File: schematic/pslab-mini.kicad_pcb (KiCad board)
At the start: 4 copper layers, 85 x 56 mm, 182 parts, among them J1 USB_C_Receptacle_USB2.0_16P, J2 BAT, J3 Conn_Coaxial, J4 Conn_Coaxial, J5 Conn_02x16_Odd_Even, J6 Conn_01x15_Socket, J7 Conn_02x03_Top_Bottom, Q1 MMBT3904, Q2 MMBT3904, SW1 Reset, SW4 Power, U1 AMS1117-3.3, U10 OPA356AIDBVR, U11 ESP32-C3, U12 W25Q32JV, U2 MT2496, U3 IP5189T, U4 SP0503BAHT, U5 OPA356AIDBVR, U6 OPA356AIDBVR, U7 TLV9001IDCK, U8 STM32H563RIT6, U9 OPA356AIDBVR, X1 32kHz768, Y1 Crystal_25MHz, Y2 40MHz

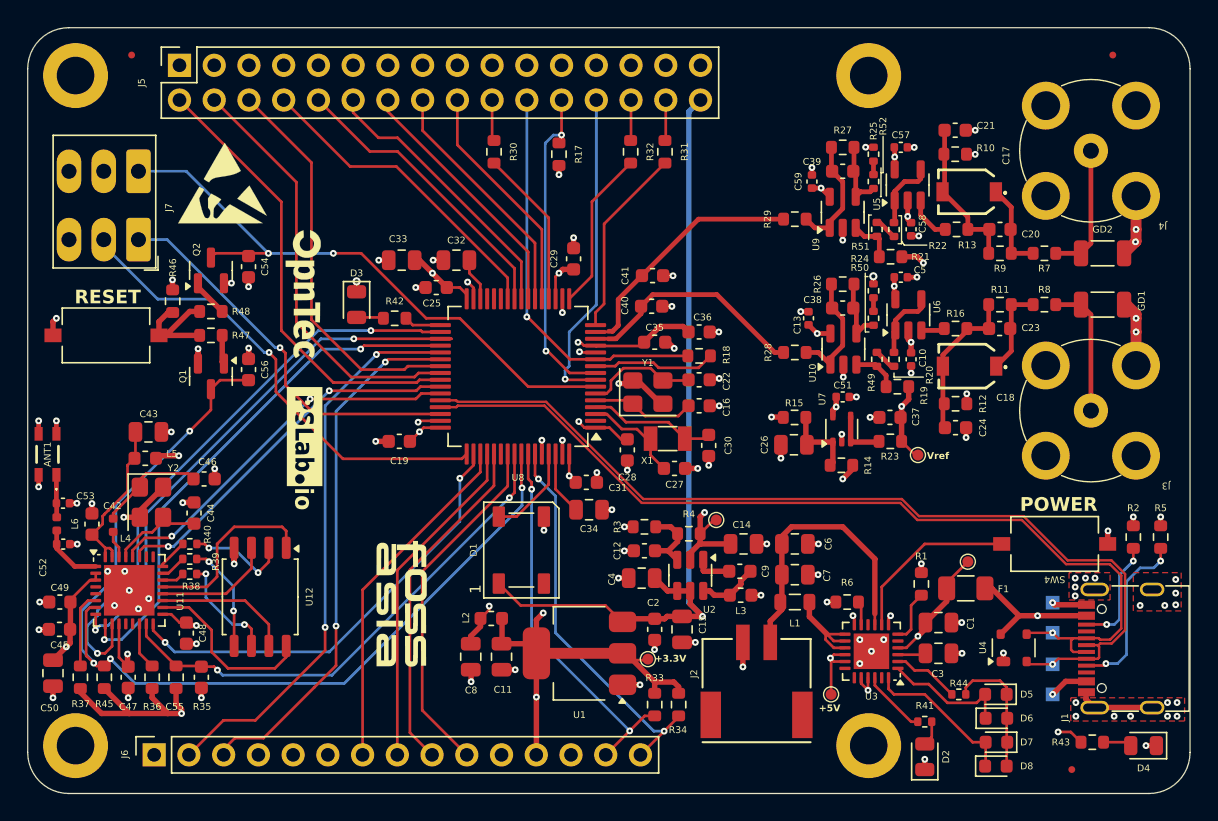
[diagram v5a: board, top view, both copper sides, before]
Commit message: updated_vias (#55)
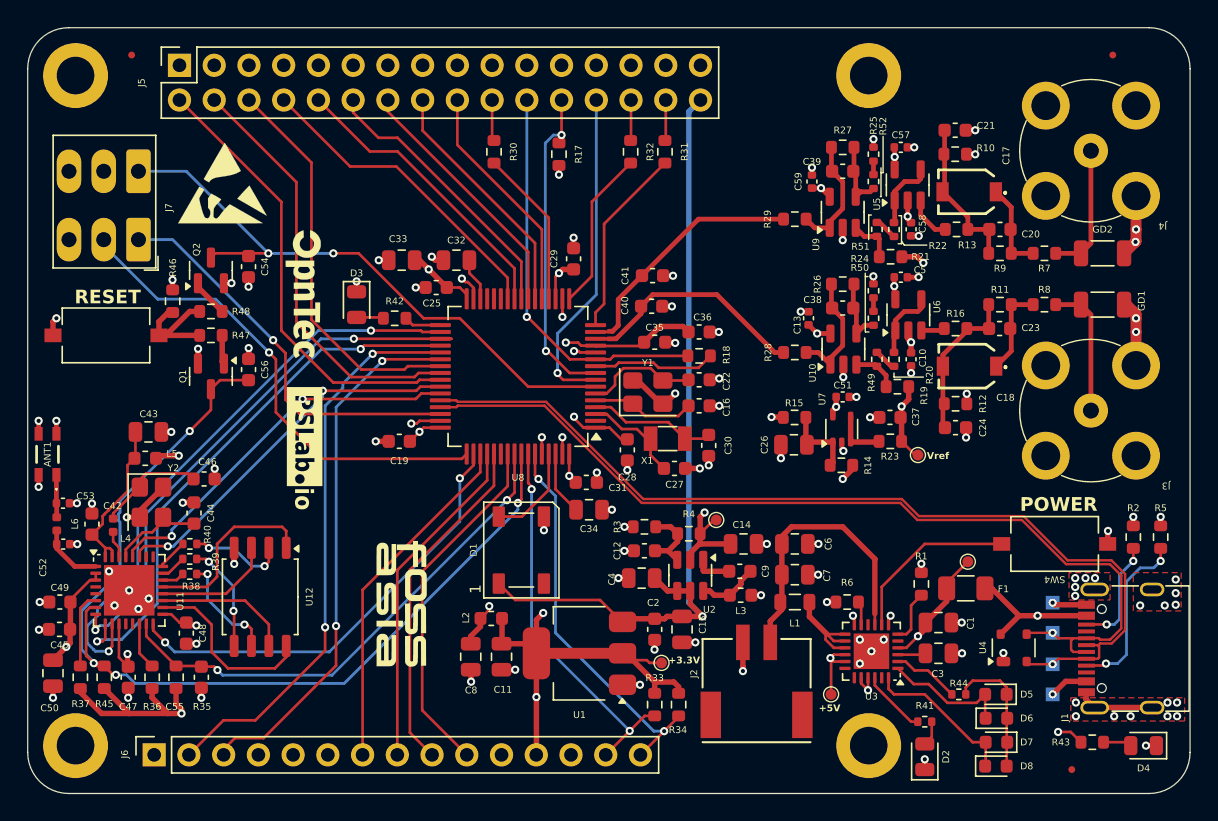
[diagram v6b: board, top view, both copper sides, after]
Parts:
- moved TP1 1.04 mm to (126.0, 99.7)
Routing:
- net GND: track 96.7 -> 100.1 mm, vias 124 -> 123
- net +3V3: track 322.3 -> 323.7 mm
- net /ESP_SPI2_MOSI: track 38.5 -> 39.7 mm
- net /SWCLK: track 34.9 -> 35.8 mm
- net /SWDIO: track 28.7 -> 29.4 mm
- net /VOL: track 23.9 -> 24.5 mm

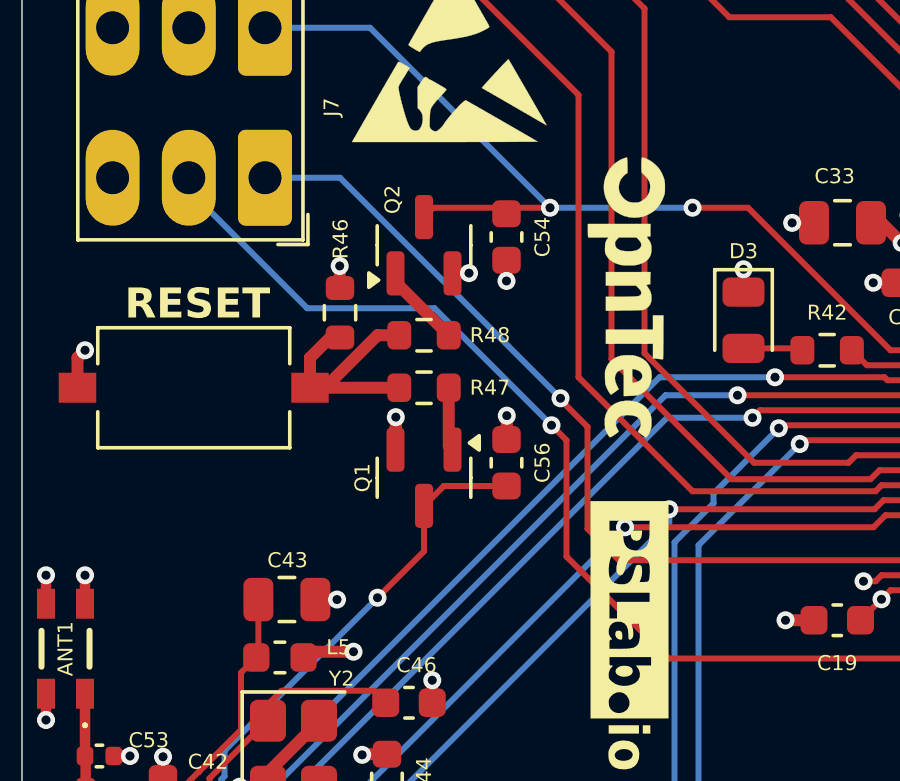
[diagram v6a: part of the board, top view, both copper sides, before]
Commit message: fixing footprints
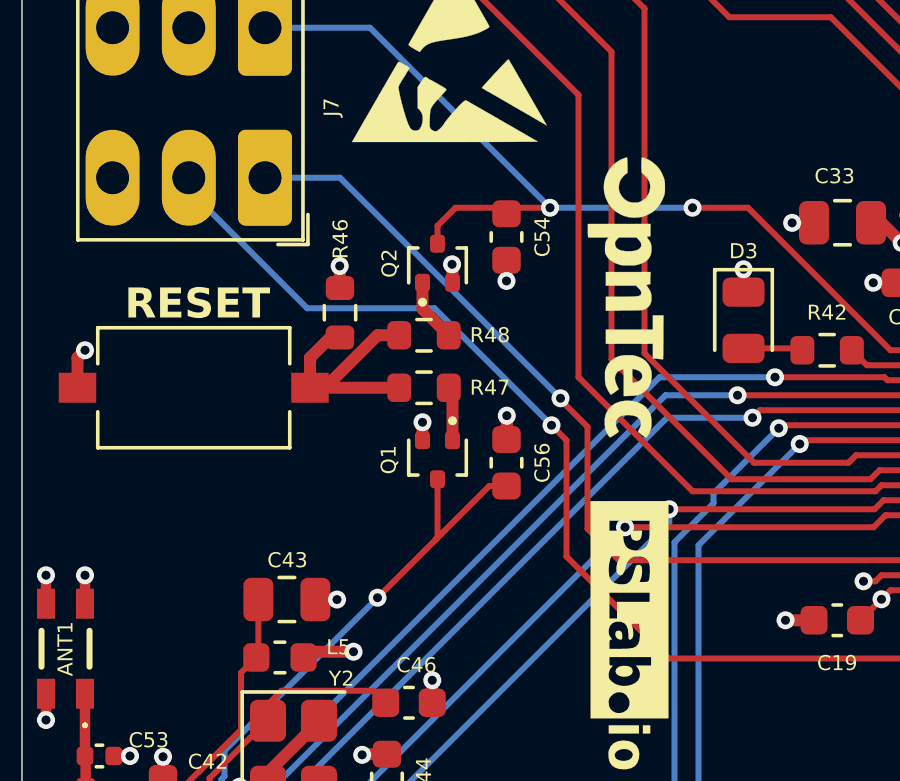
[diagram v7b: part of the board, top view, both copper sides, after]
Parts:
- Q1, Q2: footprint Package_TO_SOT_SMD:SOT-23 -> pslab-mini:SOT-416
- moved Q1 0.75 mm to (93.5, 78.2)
- moved Q2 0.75 mm to (93.5, 71.6)
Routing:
- net /ESP_EN: track 73.3 -> 74.6 mm
- net Net-(Q2-B): track 2.80 -> 2.11 mm
